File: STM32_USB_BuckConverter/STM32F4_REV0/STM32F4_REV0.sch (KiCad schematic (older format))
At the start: 35 parts

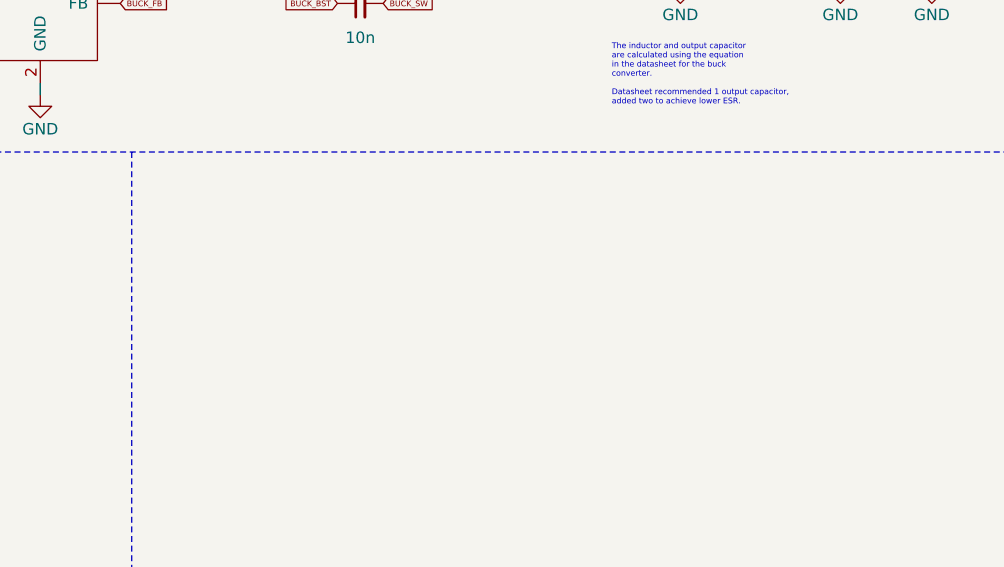
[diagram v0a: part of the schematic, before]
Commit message: Added footprints for power connectors and Serial wire debug connector
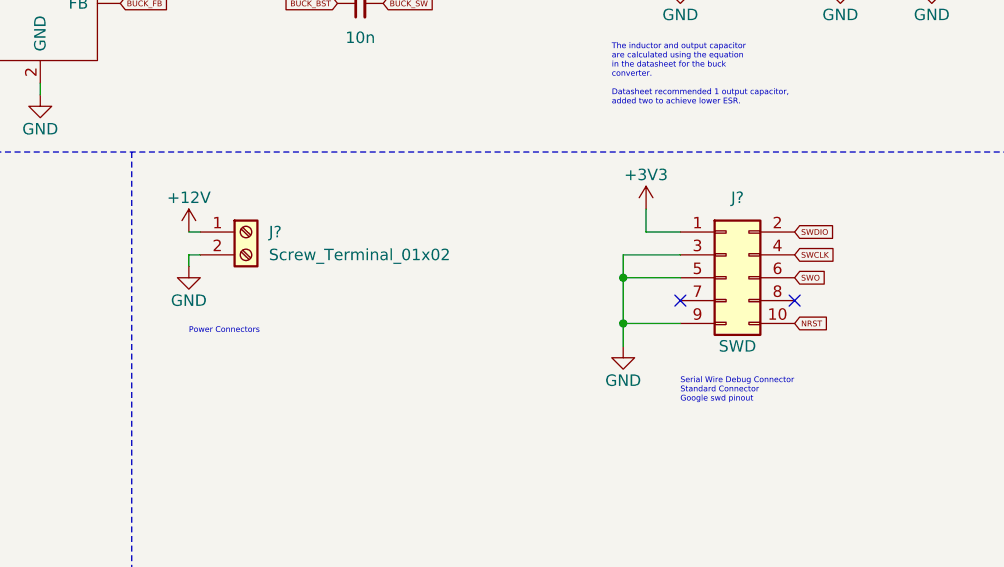
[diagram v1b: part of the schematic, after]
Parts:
- added J?: Screw_Terminal_01x02, symbol Connector:Screw_Terminal_01x02
- added J?: SWD, symbol Connector_Generic:Conn_02x05_Odd_Even
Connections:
- net +12V: now also J?.1 (Pin_1)
- net +3V3: now also J?.1 (Pin_1)
- net GND: now also J?.2 (Pin_2), J?.3 (Pin_3), J?.5 (Pin_5), J?.9 (Pin_9)
- net NRST: now also J?.10 (Pin_10)
- net SWCLK: now also J?.4 (Pin_4)
- net SWDIO: now also J?.2 (Pin_2)
- net SWO: now also J?.6 (Pin_6)
- no-connect marks 39 -> 41
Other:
- note added: "Power Connectors"
- note added: "Serial Wire Debug Connector \nStandard Connector\nGoogle swd pinout"
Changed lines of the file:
@@
 Wire Wire Line
 	1250 1050 1450 1050
+$Comp
+L Connector:Screw_Terminal_01x02 J?
+U 1 1 6080669D
+P 6250 2350
+F 0 "J?" H 6350 2350 50  0000 L CNN
+F 1 "Screw_Terminal_01x02" H 6350 2250 50  0000 L CNN
+F 2 "" H 6250 2350 50  0001 C CNN
+F 3 "~" H 6250 2350 50  0001 C CNN
+	1    6250 2350
+	1    0    0    -1
+$EndComp
+$Comp
+L power:GND #PWR?
+U 1 1 60806FA0
+P 6000 2500
+F 0 "#PWR?" H 6000 2250 50  0001 C CNN
+F 1 "GND" H 6000 2350 50  0000 C CNN
+F 2 "" H 6000 2500 50  0001 C CNN
+F 3 "" H 6000 2500 50  0001 C CNN
+	1    6000 2500
+	-1   0    0    -1
+$EndComp
+Wire Wire Line
+	6000 2500 6000 2450
+Wire Wire Line
+	6000 2450 6050 2450
+$Comp
+L power:+12V #PWR?
+U 1 1 6080AC53
+P 6000 2350
+F 0 "#PWR?" H 6000 2200 50  0001 C CNN
+F 1 "+12V" H 6000 2500 50  0000 C CNN
+F 2 "" H 6000 2350 50  0001 C CNN
+F 3 "" H 6000 2350 50  0001 C CNN
+	1    6000 2350
+	1    0    0    -1
+$EndComp
+Wire Wire Line
+	6050 2350 6000 2350
+$Comp
+L Connector_Generic:Conn_02x05_Odd_Even J?
+U 1 1 60811133
+P 8350 2550
+F 0 "J?" H 8400 2900 50  0000 C CNN
+F 1 "SWD" H 8400 2250 50  0000 C CNN
+F 2 "" H 8350 2550 50  0001 C CNN
+F 3 "~" H 8350 2550 50  0001 C CNN
+	1    8350 2550
+	1    0    0    -1
+$EndComp
+Text Notes 6000 2800 0    25   ~ 0
+Power Connectors
+Text Notes 8150 3100 0    25   ~ 0
+Serial Wire Debug Connector \nStandard Connector\nGoogle swd pinout
+$Comp
+L power:+3V3 #PWR?
+U 1 1 6081F9A1
+P 8000 2250
+F 0 "#PWR?" H 8000 2100 50  0001 C CNN
+F 1 "+3V3" H 8000 2400 50  0000 C CNN
+F 2 "" H 8000 2250 50  0001 C CNN
+F 3 "" H 8000 2250 50  0001 C CNN
+	1    8000 2250
+	1    0    0    -1
+$EndComp
+Wire Wire Line
+	8000 2250 8000 2350
+Wire Wire Line
+	8000 2350 8150 2350
+$Comp
+L power:GND #PWR?
+U 1 1 6083A068
+P 7900 2850
+F 0 "#PWR?" H 7900 2600 50  0001 C CNN
+F 1 "GND" H 7900 2700 50  0000 C CNN
+F 2 "" H 7900 2850 50  0001 C CNN
+F 3 "" H 7900 2850 50  0001 C CNN
+	1    7900 2850
+	-1   0    0    -1
+$EndComp
+Wire Wire Line
+	8150 2450 7900 2450
+Wire Wire Line
+	7900 2550 8150 2550
+Wire Wire Line
+	7900 2450 7900 2550
+Connection ~ 7900 2550
+Wire Wire Line
+	7900 2550 7900 2750
+Wire Wire Line
+	8150 2750 7900 2750
+Connection ~ 7900 2750
+Wire Wire Line
+	7900 2750 7900 2850
+NoConn ~ 8150 2650
+Text GLabel 8650 2350 2    25   Input ~ 0
+SWDIO
+Text GLabel 8650 2450 2    25   Input ~ 0
+SWCLK
+Text GLabel 8650 2550 2    25   Input ~ 0
+SWO
+Text GLabel 8650 2750 2    25   Input ~ 0
+NRST
+NoConn ~ 8650 2650
 $EndSCHEMATC

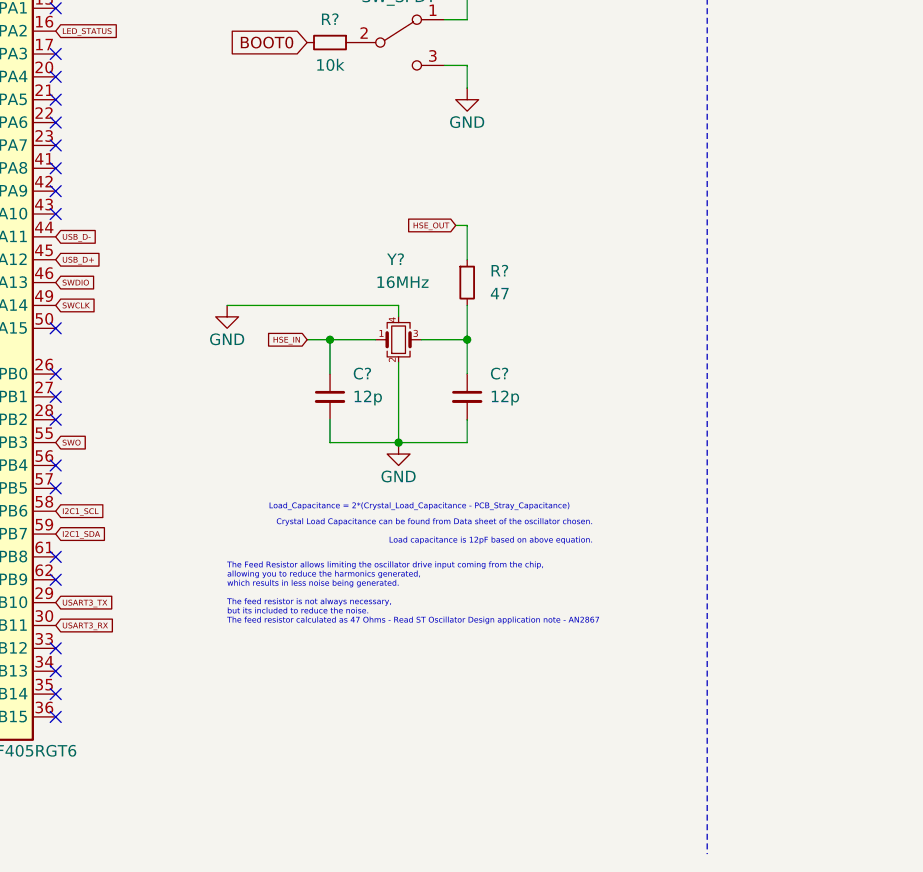
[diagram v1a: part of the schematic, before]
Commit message: Added pull-up resistors to I2C data and clock line.
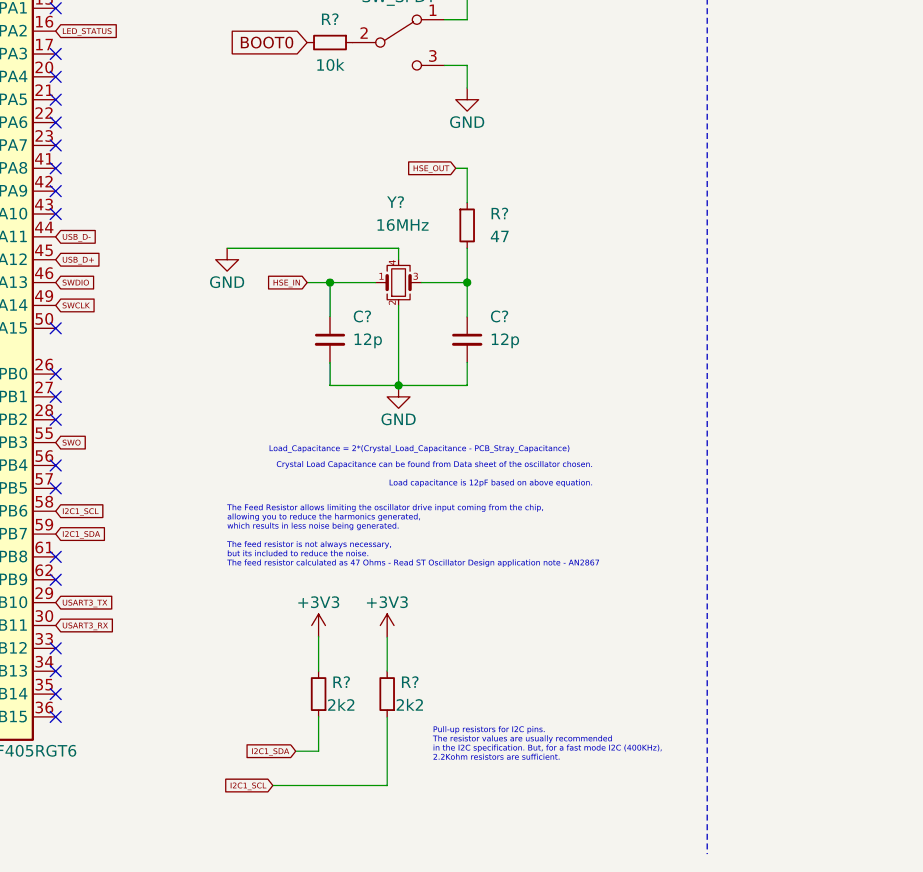
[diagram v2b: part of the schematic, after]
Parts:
- added R? (x2): 2k2, symbol Device:R_Small
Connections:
- net +3V3: now also R?.2, R?.2
- net I2C1_SCL: now also R?.1
- net I2C1_SDA: now also R?.1
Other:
- note added: "Pull-up resistors for I2C pins. \nThe resistor values are usually recommended\nin the I2C specification. But, for a fast mode I2C (400KHz), \n2.2Kohm resistors are sufficient."
- moved on the sheet: C?, R?, Y?
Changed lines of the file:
@@
 L Device:Crystal_GND24_Small Y?
 U 1 1 6062C86D
-P 4400 5550
-F 0 "Y?" H 4350 5900 50  0000 L CNN
-F 1 "16MHz" H 4300 5800 50  0000 L CNN
-F 2 "" H 4400 5550 50  0001 C CNN
-F 3 "~" H 4400 5550 50  0001 C CNN
-	1    4400 5550
+P 4400 5300
+F 0 "Y?" H 4350 5650 50  0000 L CNN
+F 1 "16MHz" H 4300 5550 50  0000 L CNN
+F 2 "" H 4400 5300 50  0001 C CNN
+F 3 "~" H 4400 5300 50  0001 C CNN
+	1    4400 5300
 	1    0    0    -1
 $EndComp
@@
 L Device:C_Small C?
 U 1 1 6062EA12
-P 4100 5800
-F 0 "C?" H 4200 5900 50  0000 L CNN
-F 1 "12p" H 4200 5800 50  0000 L CNN
-F 2 "" H 4100 5800 50  0001 C CNN
-F 3 "~" H 4100 5800 50  0001 C CNN
-	1    4100 5800
-	1    0    0    -1
-$EndComp
-Wire Wire Line
-	4100 5550 4300 5550
-Wire Wire Line
-	4500 5550 4700 5550
-Wire Wire Line
-	4700 5550 4700 5700
+P 4100 5550
+F 0 "C?" H 4200 5650 50  0000 L CNN
+F 1 "12p" H 4200 5550 50  0000 L CNN
+F 2 "" H 4100 5550 50  0001 C CNN
+F 3 "~" H 4100 5550 50  0001 C CNN
+	1    4100 5550
+	1    0    0    -1
+$EndComp
+Wire Wire Line
+	4100 5300 4300 5300
+Wire Wire Line
+	4500 5300 4700 5300
+Wire Wire Line
+	4700 5300 4700 5450
 $Comp
 L power:GND #PWR?
 U 1 1 60632B61
-P 4400 6000
-F 0 "#PWR?" H 4400 5750 50  0001 C CNN
-F 1 "GND" H 4400 5850 50  0000 C CNN
-F 2 "" H 4400 6000 50  0001 C CNN
-F 3 "" H 4400 6000 50  0001 C CNN
-	1    4400 6000
-	1    0    0    -1
-$EndComp
-Wire Wire Line
-	4100 5900 4100 6000
-Wire Wire Line
-	4100 6000 4400 6000
-Wire Wire Line
-	4400 6000 4700 6000
-Wire Wire Line
-	4700 6000 4700 5900
-Connection ~ 4400 6000
-Wire Wire Line
-	4400 5650 4400 6000
+P 4400 5750
+F 0 "#PWR?" H 4400 5500 50  0001 C CNN
+F 1 "GND" H 4400 5600 50  0000 C CNN
+F 2 "" H 4400 5750 50  0001 C CNN
+F 3 "" H 4400 5750 50  0001 C CNN
+	1    4400 5750
+	1    0    0    -1
+$EndComp
+Wire Wire Line
+	4100 5650 4100 5750
+Wire Wire Line
+	4100 5750 4400 5750
+Wire Wire Line
+	4400 5750 4700 5750
+Wire Wire Line
+	4700 5750 4700 5650
+Connection ~ 4400 5750
+Wire Wire Line
+	4400 5400 4400 5750
 $Comp
 L power:GND #PWR?
 U 1 1 60637BC4
-P 3650 5400
-F 0 "#PWR?" H 3650 5150 50  0001 C CNN
-F 1 "GND" H 3650 5250 50  0000 C CNN
-F 2 "" H 3650 5400 50  0001 C CNN
-F 3 "" H 3650 5400 50  0001 C CNN
-	1    3650 5400
-	1    0    0    -1
-$EndComp
-Wire Wire Line
-	4400 5400 4400 5450
+P 3650 5150
+F 0 "#PWR?" H 3650 4900 50  0001 C CNN
+F 1 "GND" H 3650 5000 50  0000 C CNN
+F 2 "" H 3650 5150 50  0001 C CNN
+F 3 "" H 3650 5150 50  0001 C CNN
+	1    3650 5150
+	1    0    0    -1
+$EndComp
+Wire Wire Line
+	4400 5150 4400 5200
 $Comp
 L Device:R_Small R?
 U 1 1 6063C414
-P 4700 5300
-F 0 "R?" H 4800 5350 50  0000 L CNN
-F 1 "47" H 4800 5250 50  0000 L CNN
-F 2 "" H 4700 5300 50  0001 C CNN
-F 3 "~" H 4700 5300 50  0001 C CNN
-	1    4700 5300
-	1    0    0    -1
-$EndComp
-Wire Wire Line
-	4700 5400 4700 5550
-Connection ~ 4700 5550
-Text GLabel 4000 5550 0    25   Input ~ 0
+P 4700 5050
+F 0 "R?" H 4800 5100 50  0000 L CNN
+F 1 "47" H 4800 5000 50  0000 L CNN
+F 2 "" H 4700 5050 50  0001 C CNN
+F 3 "~" H 4700 5050 50  0001 C CNN
+	1    4700 5050
+	1    0    0    -1
+$EndComp
+Wire Wire Line
+	4700 5150 4700 5300
+Connection ~ 4700 5300
+Text GLabel 4000 5300 0    25   Input ~ 0
 HSE_IN
 Wire Wire Line
-	4100 5700 4100 5550
-Wire Wire Line
-	3650 5400 4400 5400
-Wire Wire Line
-	4000 5550 4100 5550
-Connection ~ 4100 5550
-Text GLabel 4650 5050 0    25   Input ~ 0
+	4100 5450 4100 5300
+Wire Wire Line
+	3650 5150 4400 5150
+Wire Wire Line
+	4000 5300 4100 5300
+Connection ~ 4100 5300
+Text GLabel 4650 4800 0    25   Input ~ 0
 HSE_OUT
 Wire Wire Line
-	4650 5050 4700 5050
-Wire Wire Line
-	4700 5050 4700 5200
-Text Notes 5150 6300 2    25   ~ 0
+	4650 4800 4700 4800
+Wire Wire Line
+	4700 4800 4700 4950
+Text Notes 5150 6050 2    25   ~ 0
 Load_Capacitance = 2*(Crystal_Load_Capacitance - PCB_Stray_Capacitance)
-Text Notes 5250 6450 2    25   ~ 0
+Text Notes 5250 6200 2    25   ~ 0
 Crystal Load Capacitance can be found from Data sheet of the oscillator chosen. \n\nLoad capacitance is 12pF based on above equation.
 Text Notes 3750 3800 0    25   ~ 0
@@
 Text Notes 1600 3900 2    25   ~ 0
 NRST allows hard reseting the\n chip by driving this pin low.
-Text Notes 3650 6800 0    25   ~ 0
+Text Notes 3650 6550 0    25   ~ 0
 The Feed Resistor allows limiting the oscillator drive input coming from the chip,\nallowing you to reduce the harmonics generated,  \nwhich results in less noise being generated. \n\nThe feed resistor is not always necessary, \nbut its included to reduce the noise. \nThe feed resistor calculated as 47 Ohms - Read ST Oscillator Design application note - AN2867
 $Comp
 L Device:C_Small C?
 U 1 1 6062DC99
-P 4700 5800
-F 0 "C?" H 4800 5900 50  0000 L CNN
-F 1 "12p" H 4800 5800 50  0000 L CNN
-F 2 "" H 4700 5800 50  0001 C CNN
-F 3 "~" H 4700 5800 50  0001 C CNN
-	1    4700 5800
+P 4700 5550
+F 0 "C?" H 4800 5650 50  0000 L CNN
+F 1 "12p" H 4800 5550 50  0000 L CNN
+F 2 "" H 4700 5550 50  0001 C CNN
+F 3 "~" H 4700 5550 50  0001 C CNN
+	1    4700 5550
 	1    0    0    -1
 $EndComp
@@
 NRST
 NoConn ~ 8650 2650
+$Comp
+L Device:R_Small R?
+U 1 1 6085E3D5
+P 4050 7100
+F 0 "R?" H 3950 7050 50  0000 C CNN
+F 1 "2k2" H 3950 7150 50  0000 C CNN
+F 2 "" H 4050 7100 50  0001 C CNN
+F 3 "~" H 4050 7100 50  0001 C CNN
+	1    4050 7100
+	-1   0    0    1
+$EndComp
+$Comp
+L Device:R_Small R?
+U 1 1 6085E794
+P 4350 7100
+F 0 "R?" H 4250 7050 50  0000 C CNN
+F 1 "2k2" H 4250 7150 50  0000 C CNN
+F 2 "" H 4350 7100 50  0001 C CNN
+F 3 "~" H 4350 7100 50  0001 C CNN
+	1    4350 7100
+	-1   0    0    1
+$EndComp
+$Comp
+L power:+3V3 #PWR?
+U 1 1 6085E9D1
+P 4050 6850
+F 0 "#PWR?" H 4050 6700 50  0001 C CNN
+F 1 "+3V3" H 4050 7000 50  0000 C CNN
+F 2 "" H 4050 6850 50  0001 C CNN
+F 3 "" H 4050 6850 50  0001 C CNN
+	1    4050 6850
+	1    0    0    -1
+$EndComp
+$Comp
+L power:+3V3 #PWR?
+U 1 1 6085EFB9
+P 4350 6850
+F 0 "#PWR?" H 4350 6700 50  0001 C CNN
+F 1 "+3V3" H 4350 7000 50  0000 C CNN
+F 2 "" H 4350 6850 50  0001 C CNN
+F 3 "" H 4350 6850 50  0001 C CNN
+	1    4350 6850
+	1    0    0    -1
+$EndComp
+Wire Wire Line
+	4050 6850 4050 7000
+Wire Wire Line
+	4350 6850 4350 7000
+Text GLabel 3850 7500 0    25   Input ~ 0
+I2C1_SCL
+Text GLabel 3950 7350 0    25   Input ~ 0
+I2C1_SDA
+Wire Wire Line
+	3950 7350 4050 7350
+Wire Wire Line
+	4050 7350 4050 7200
+Wire Wire Line
+	3850 7500 4350 7500
+Wire Wire Line
+	4350 7500 4350 7200
+Text Notes 4550 7400 0    25   ~ 0
+Pull-up resistors for I2C pins. \nThe resistor values are usually recommended\nin the I2C specification. But, for a fast mode I2C (400KHz), \n2.2Kohm resistors are sufficient.
 $EndSCHEMATC

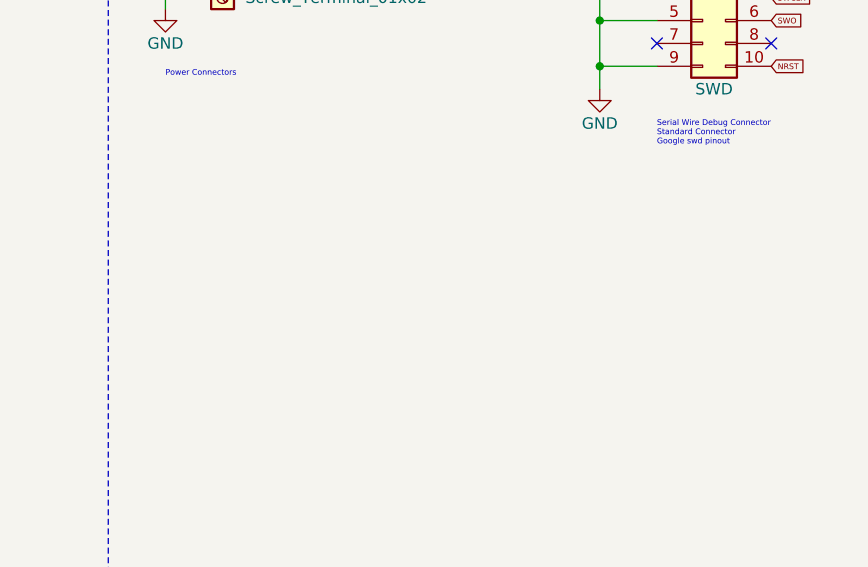
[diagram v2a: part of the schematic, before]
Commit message: Added connectors for I2C and UART modules.
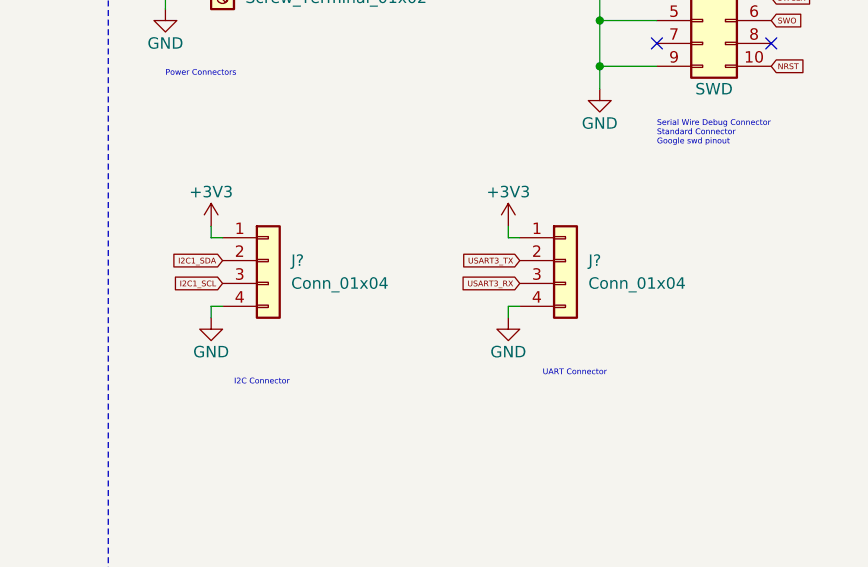
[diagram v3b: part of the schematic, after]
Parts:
- added J? (x2): Conn_01x04, symbol Connector_Generic:Conn_01x04
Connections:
- net +3V3: now also J?.1 (Pin_1), J?.1 (Pin_1)
- net GND: now also J?.4 (Pin_4), J?.4 (Pin_4)
- net I2C1_SCL: now also J?.3 (Pin_3)
- net I2C1_SDA: now also J?.2 (Pin_2)
- net USART3_RX: now also J?.3 (Pin_3)
- net USART3_TX: now also J?.2 (Pin_2)
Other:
- note added: "I2C Connector"
- note added: "UART Connector\n\n"
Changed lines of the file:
@@
 Text Notes 4550 7400 0    25   ~ 0
 Pull-up resistors for I2C pins. \nThe resistor values are usually recommended\nin the I2C specification. But, for a fast mode I2C (400KHz), \n2.2Kohm resistors are sufficient.
+$Comp
+L Connector_Generic:Conn_01x04 J?
+U 1 1 6087753B
+P 6450 3600
+F 0 "J?" H 6550 3600 50  0000 L CNN
+F 1 "Conn_01x04" H 6550 3500 50  0000 L CNN
+F 2 "" H 6450 3600 50  0001 C CNN
+F 3 "~" H 6450 3600 50  0001 C CNN
+	1    6450 3600
+	1    0    0    -1
+$EndComp
+$Comp
+L power:+3V3 #PWR?
+U 1 1 6087805C
+P 6200 3450
+F 0 "#PWR?" H 6200 3300 50  0001 C CNN
+F 1 "+3V3" H 6200 3600 50  0000 C CNN
+F 2 "" H 6200 3450 50  0001 C CNN
+F 3 "" H 6200 3450 50  0001 C CNN
+	1    6200 3450
+	1    0    0    -1
+$EndComp
+$Comp
+L power:GND #PWR?
+U 1 1 608789B9
+P 6200 3850
+F 0 "#PWR?" H 6200 3600 50  0001 C CNN
+F 1 "GND" H 6200 3700 50  0000 C CNN
+F 2 "" H 6200 3850 50  0001 C CNN
+F 3 "" H 6200 3850 50  0001 C CNN
+	1    6200 3850
+	-1   0    0    -1
+$EndComp
+Wire Wire Line
+	6250 3800 6200 3800
+Wire Wire Line
+	6200 3800 6200 3850
+Wire Wire Line
+	6200 3450 6200 3500
+Wire Wire Line
+	6200 3500 6250 3500
+Text GLabel 6250 3700 0    25   Input ~ 0
+I2C1_SCL
+Text GLabel 6250 3600 0    25   Input ~ 0
+I2C1_SDA
+Text Notes 6300 4150 0    25   ~ 0
+I2C Connector
+$Comp
+L Connector_Generic:Conn_01x04 J?
+U 1 1 6089BD8D
+P 7750 3600
+F 0 "J?" H 7850 3600 50  0000 L CNN
+F 1 "Conn_01x04" H 7850 3500 50  0000 L CNN
+F 2 "" H 7750 3600 50  0001 C CNN
+F 3 "~" H 7750 3600 50  0001 C CNN
+	1    7750 3600
+	1    0    0    -1
+$EndComp
+$Comp
+L power:+3V3 #PWR?
+U 1 1 6089D097
+P 7500 3450
+F 0 "#PWR?" H 7500 3300 50  0001 C CNN
+F 1 "+3V3" H 7500 3600 50  0000 C CNN
+F 2 "" H 7500 3450 50  0001 C CNN
+F 3 "" H 7500 3450 50  0001 C CNN
+	1    7500 3450
+	1    0    0    -1
+$EndComp
+$Comp
+L power:GND #PWR?
+U 1 1 6089DB8B
+P 7500 3850
+F 0 "#PWR?" H 7500 3600 50  0001 C CNN
+F 1 "GND" H 7500 3700 50  0000 C CNN
+F 2 "" H 7500 3850 50  0001 C CNN
+F 3 "" H 7500 3850 50  0001 C CNN
+	1    7500 3850
+	-1   0    0    -1
+$EndComp
+Wire Wire Line
+	7500 3450 7500 3500
+Wire Wire Line
+	7500 3500 7550 3500
+Wire Wire Line
+	7500 3850 7500 3800
+Wire Wire Line
+	7500 3800 7550 3800
+Text GLabel 7550 3600 0    25   Input ~ 0
+USART3_TX
+Text GLabel 7550 3700 0    25   Input ~ 0
+USART3_RX
+Text Notes 7650 4150 0    25   ~ 0
+UART Connector\n\n
 $EndSCHEMATC
